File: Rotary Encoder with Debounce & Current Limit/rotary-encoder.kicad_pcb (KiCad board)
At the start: 2 copper layers, 27.9 x 23.4 mm, 20 parts, among them J1 CONN_01X05, J2 CONN_01X05, U1 74HC14

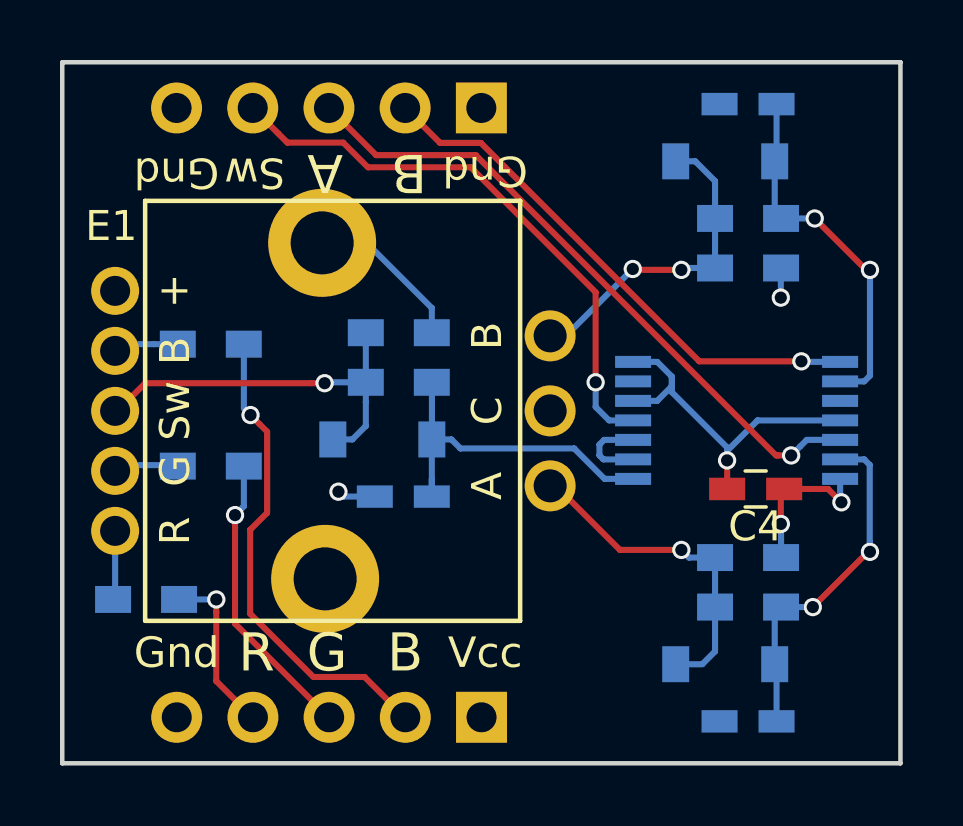
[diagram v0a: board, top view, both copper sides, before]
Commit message: Version 0.4 - added version and title text to back side
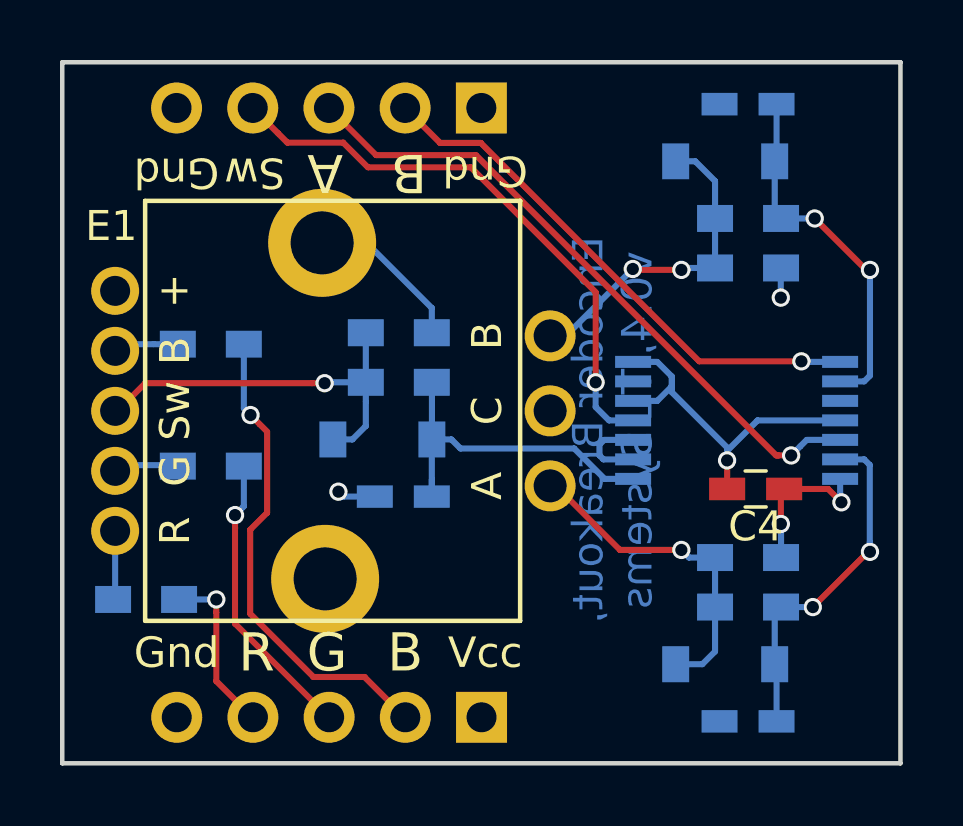
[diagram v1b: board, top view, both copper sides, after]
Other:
- board text added: "Encoder Breakout, v0.4, TL Systems"
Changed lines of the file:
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@@
     (links 46)
     (no_connects 0)
-    (area 104.856599 91.067399 132.946601 114.585401)
+    (area 104.856599 90.638199 132.946601 117.1646)
     (thickness 1.6)
-    (drawings 24)
+    (drawings 25)
     (tracks 165)
     (zones 0)
@@
   )
   (page A4)
+  (title_block
+    (title "Rotary Encoder w/Debounce & LEDs Breakout Board")
+    (date 2017-12-15)
+    (rev v0.4)
+    (company "TL Systems")
+  )
   (layers
     (0 F.Cu signal)
@@
     )
   )
+  (gr_text "Encoder Breakout, \nv0.4, TL Systems" (at 123.2831 103.3979 90) (layer B.Cu)
+    (effects (font (size 1.016 1.016) (thickness 0.1524)) (justify mirror))
+  )
   (gr_text Gnd (at 119.0286 94.7619 180) (layer B.SilkS)
